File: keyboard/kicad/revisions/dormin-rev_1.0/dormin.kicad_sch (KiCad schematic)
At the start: 115 parts, among them J1 Conn_01x06, J2 Conn_01x04, J3 Conn_01x05, Q1 AO3400A, Q2 AO3407A, SW1 SW_Push, SW10 SW_Push, SW11 SW_Push, SW12 SW_Push, SW13 SW_Push, SW14 SW_Push, SW15 SW_Push, SW16 SW_Push, SW17 SW_Push, SW18 SW_Push, SW19 SW_Push, SW2 SW_Push, SW20 SW_Push, SW3 SW_Push, SW4 SW_Push, SW5 SW_Push, SW6 SW_Push, SW7 SW_Push, SW8 SW_Push, SW9 SW_Push, U3 XIAO-nRF52840-Plus-SMD, U4 TPD2E2U06DCK

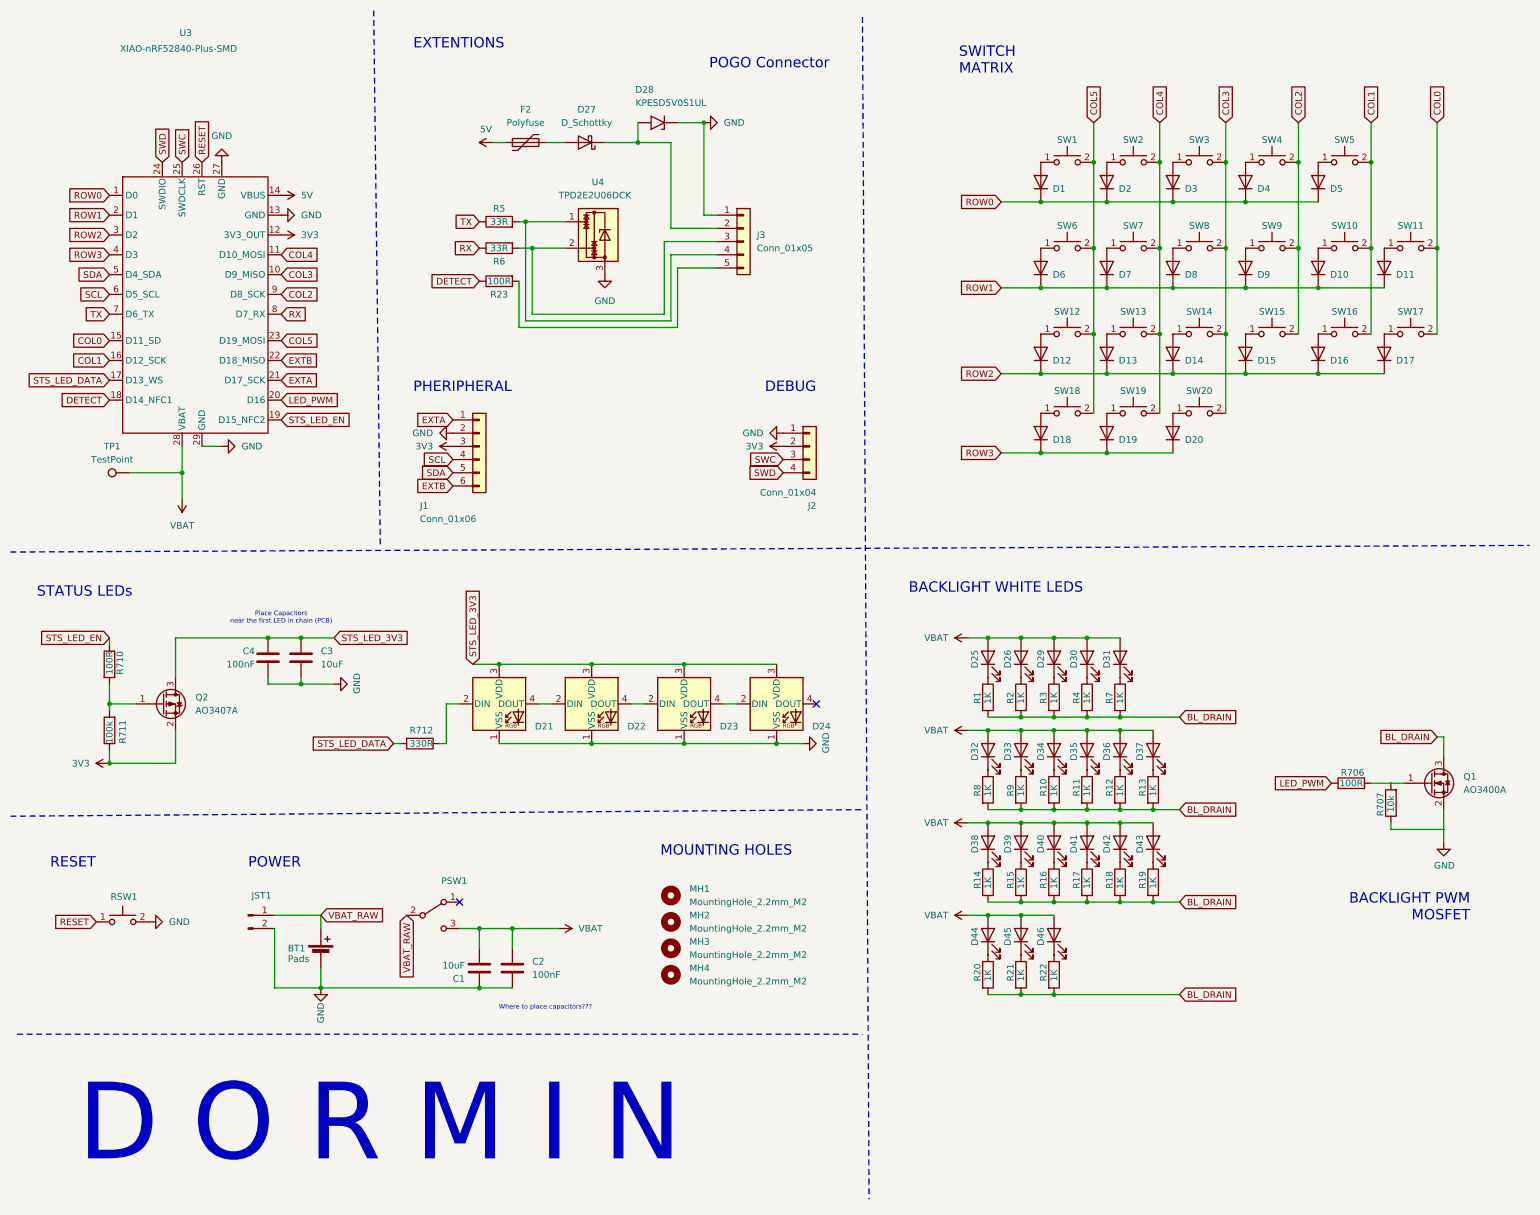
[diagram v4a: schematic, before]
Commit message: feat: improve schematics and pcb components placements
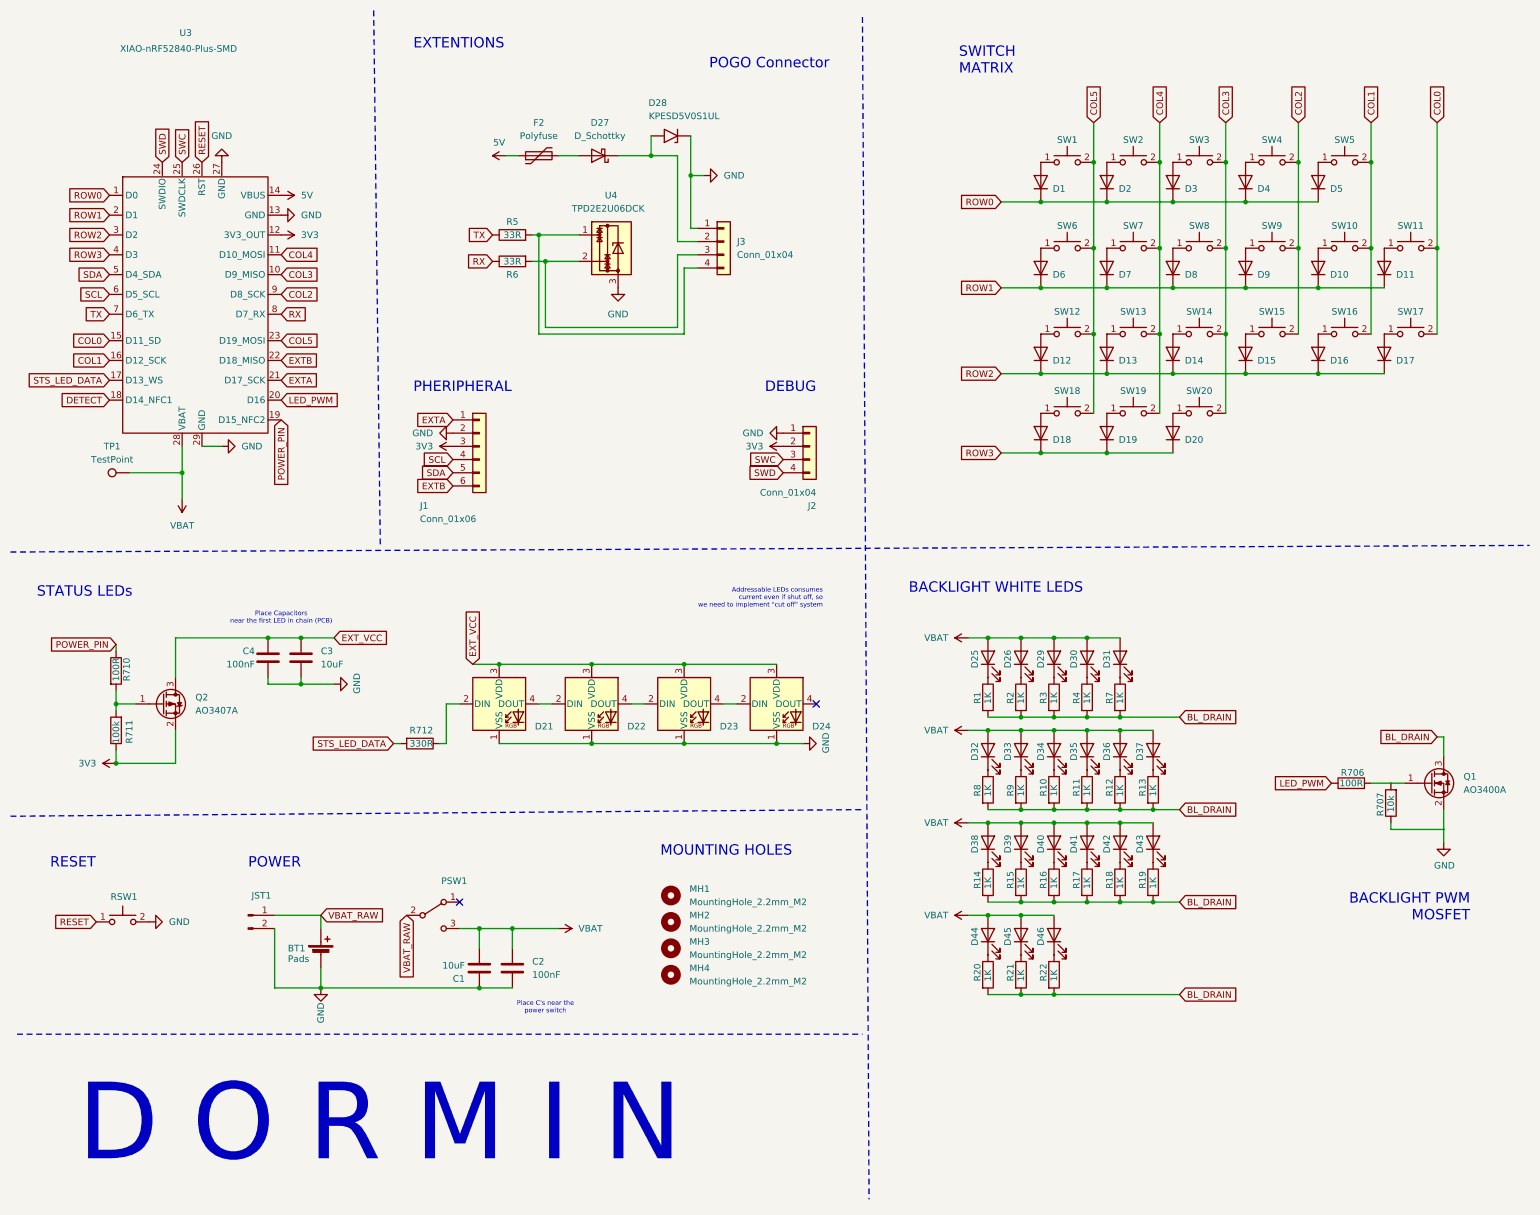
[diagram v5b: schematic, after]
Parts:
- removed J3: Conn_01x05, willkeebs_misc:SMD_Conn_1x04_P2.54mm_Vertical, symbol Connector_Generic:Conn_01x05
- removed R23: 100R, Resistor_SMD:R_0603_1608Metric, symbol Device:R
- added J3: Conn_01x04, symbol Connector_Generic:Conn_01x04
- JST1: footprint willkeebs_power:JST_1.25mm -> Connector_JST:JST_GH_SM02B-GHS-TB_1x02-1MP_P1.25mm_Horizontal; MFPN (none) -> C22074
- PSW1: footprint willkeebs_power:Switch_MSK12C02 -> PCM_marbastlib-various:SW_MSK12C02-HB; MFPN (none) -> MK-12C02-G025
- RSW1: footprint willkeebs_components:SW_Push_1P1T_XKB_TS-1187A -> Button_Switch_SMD:SW_SPST_SKQG_WithStem
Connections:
- net GND: now also J3.1 (Pin_1)
- net at R5.2, U4.1: now also J3.4 (Pin_4)
- net at D27.1 (K), D28.2 (A2): now also J3.2 (Pin_2)
- net at R6.2, U4.2: now also J3.3 (Pin_3)
- net STS_LED_3V3 renamed EXT_VCC
- net STS_LED_EN renamed POWER_PIN
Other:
- note added: "Addressable LEDs consumes current even if shut off, so we need to implement "cut off" system"
- note added: "Place C's near the power switch"
- note removed: "Where to place capacitors???"
- moved on the sheet: D27, D28, F2, R5, R6, R710, R711, U4

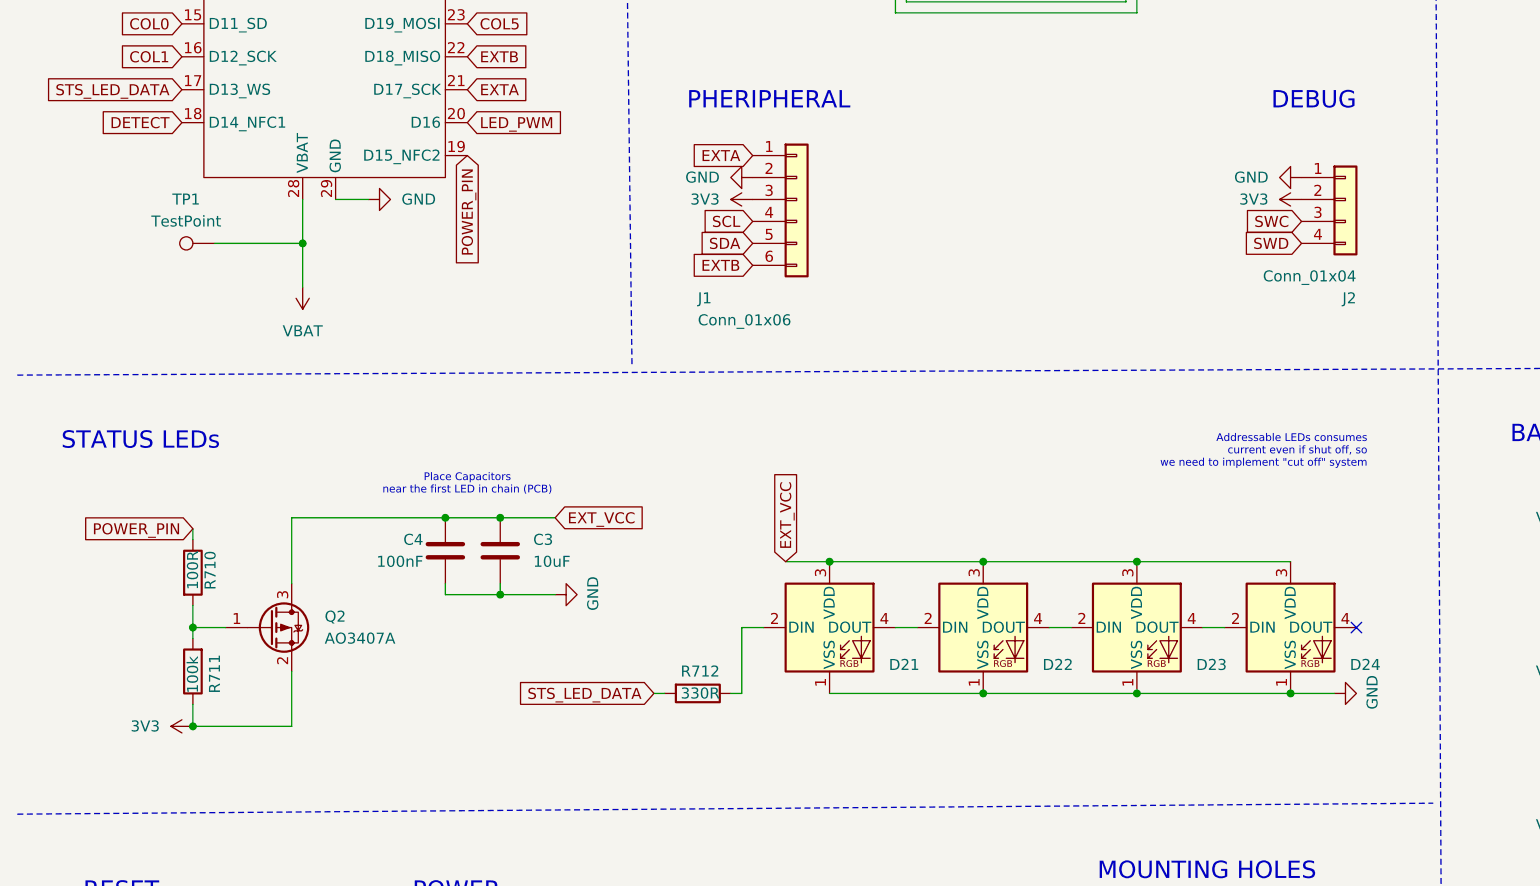
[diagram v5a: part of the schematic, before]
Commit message: feat: improve schematics and components placement
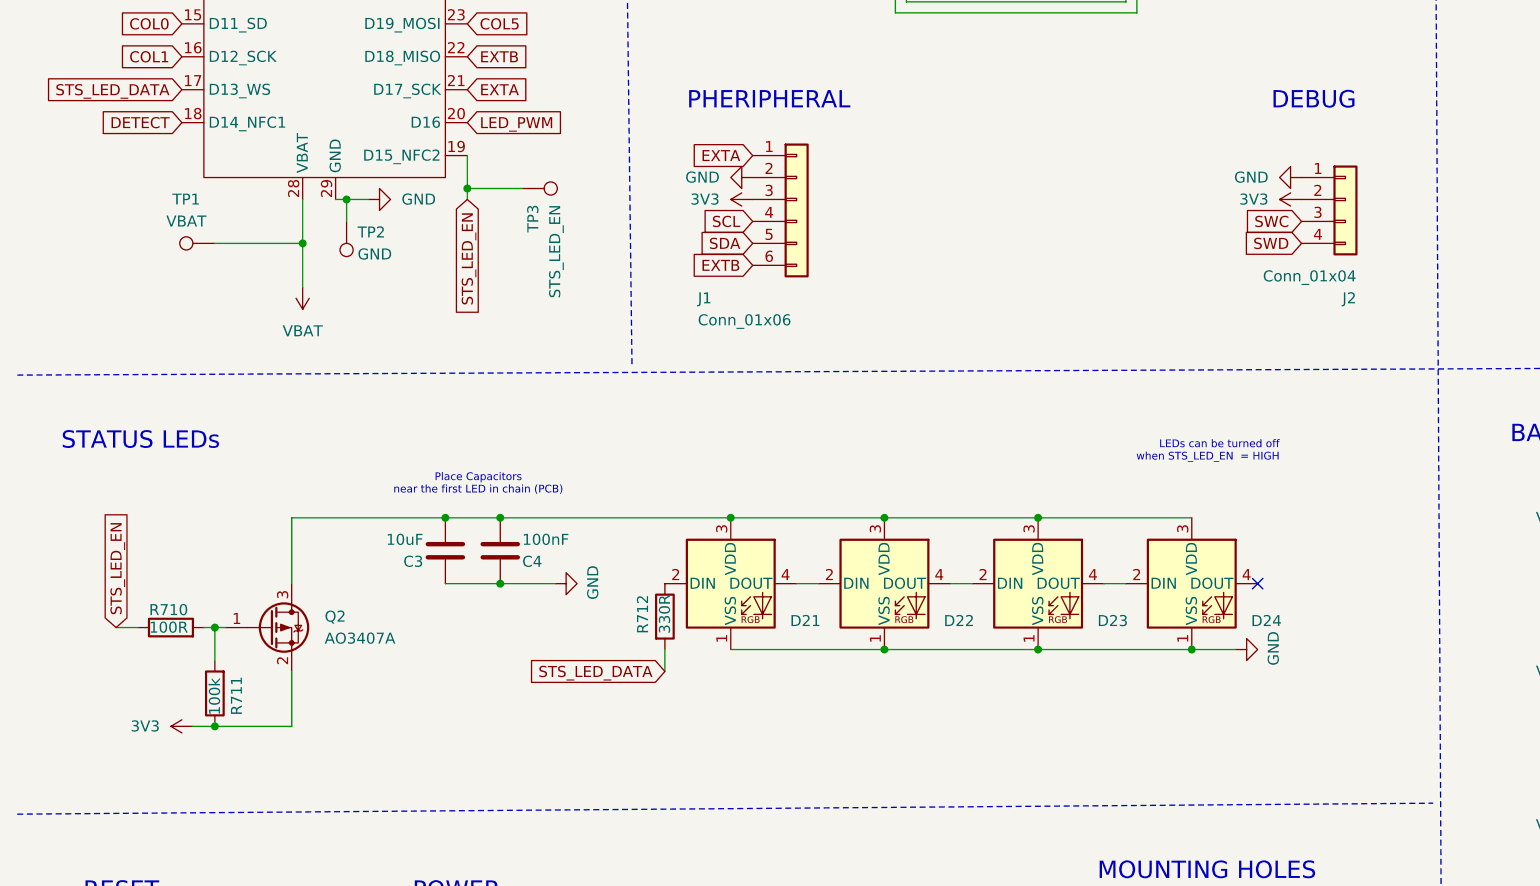
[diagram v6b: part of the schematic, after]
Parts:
- added TP2: GND, TestPoint:TestPoint_Pad_D1.0mm, symbol Connector:TestPoint
- added TP3: STS_LED_EN, TestPoint:TestPoint_Pad_D1.0mm, symbol Connector:TestPoint
- J3: footprint (none) -> willkeebs_misc:SMD_Conn_1x04_P2.54mm_Vertical
- TP1: value TestPoint -> VBAT; footprint (none) -> TestPoint:TestPoint_Pad_D1.0mm
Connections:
- net GND: now also TP2.1
- net EXT_VCC: no longer names the net of C3.2, C4.1, D21.3 (VDD), D22.3 (VDD), D23.3 (VDD), D24.3 (VDD), Q2.3 (D)
- net POWER_PIN renamed STS_LED_EN
- net STS_LED_EN: now also TP3.1
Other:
- note added: "LEDs can be turned off when STS_LED_EN = HIGH"
- note removed: "Addressable LEDs consumes current even if shut off, so we need to implement "cut off" system"
- moved on the sheet: D21, D22, D23, D24, R710, R712

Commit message: chore: added right sheet schematics
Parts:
- removed BT1: Pads, willkeebs_power:Battery_Pad, symbol Device:Battery_Cell
- removed C1, C3: 10uF, Capacitor_SMD:C_0603_1608Metric, symbol Device:C
- removed C2, C4: 100nF, Capacitor_SMD:C_0603_1608Metric, symbol Device:C
- removed D1, D10, D11, D12, D13, D14, D15, D16, D17, D18, D19, D2, D20, D3, D4, D5, D6, D7, D8, D9: 1N4148W, Diode_SMD:D_SOD-123, symbol Diode:1N4148W
- removed D21, D22, D23, D24: SK6812MINI-E, LED_SMD:LED_SK6812MINI-E_3.2x2.8mm_P1.5mm_ReverseMount, symbol LED:SK6812MINI-E
- removed D25, D26, D29, D30, D31, D32, D33, D34, D35, D36, D37, D38, D39, D40, D41, D42, D43, D44, D45, D46: LED, willkeebs_components:LED_MHT151WDT, symbol Device:LED
- removed D27: D_Schottky, Diode_SMD:D_SOD-523, symbol Device:D_Schottky
- removed D28: KPESD5V0S1UL, Diode_SMD:D_SOD-882, symbol Diode:SMF5V0A
- removed F2: Polyfuse, Fuse:Fuse_1206_3216Metric, symbol Device:Polyfuse
- removed J1: Conn_01x06, willkeebs_misc:SMD_Conn_1x06_P2.54mm_Vertical, symbol Connector_Generic:Conn_01x06
- removed J2: Conn_01x04, Connector_PinSocket_2.54mm:PinSocket_1x04_P2.54mm_Vertical, symbol Connector_Generic:Conn_01x04
- removed J3: Conn_01x04, willkeebs_misc:SMD_Conn_1x04_P2.54mm_Vertical, symbol Connector_Generic:Conn_01x04
- removed JST1: Conn_01x02_Pin, Connector_JST:JST_GH_SM02B-GHS-TB_1x02-1MP_P1.25mm_Horizontal, symbol Connector:Conn_01x02_Pin
- removed MH1, MH2, MH3, MH4: MountingHole_2.2mm_M2, MountingHole:MountingHole_2.2mm_M2, symbol Mechanical:MountingHole
- removed PSW1: SW_SPDT, PCM_marbastlib-various:SW_MSK12C02-HB, symbol Switch:SW_SPDT
- removed Q1: AO3400A, Package_TO_SOT_SMD:SOT-23, symbol Transistor_FET:AO3400A
- removed Q2: AO3407A, Package_TO_SOT_SMD:SOT-23, symbol Transistor_FET:AO3401A
- removed R1, R10, R11, R12, R13, R14, R15, R16, R17, R18, R19, R2, R20, R21, R22, R3, R4, R7, R8, R9: 1K, Resistor_SMD:R_0603_1608Metric, symbol Device:R
- removed R5, R6: 33R, Resistor_SMD:R_0603_1608Metric, symbol Device:R
- removed R706, R710: 100R, Resistor_SMD:R_0603_1608Metric, symbol Device:R
- removed R707: 10k, Resistor_SMD:R_0603_1608Metric, symbol Device:R
- removed R711: 100k, Resistor_SMD:R_0603_1608Metric, symbol Device:R
- removed R712: 330R, Resistor_SMD:R_0603_1608Metric, symbol Device:R
- removed RSW1: RSW1, Button_Switch_SMD:SW_SPST_SKQG_WithStem, symbol Switch:SW_Push
- removed SW1, SW10, SW11, SW12, SW13, SW14, SW15, SW16, SW17, SW18, SW19, SW2, SW20, SW3, SW4, SW5, SW6, SW7, SW8, SW9: SW_Push, willkeebs_keyboard:NF_LED_1206_SW_KS33_3_0_HS_1U, symbol Switch:SW_Push
- removed TP1: VBAT, TestPoint:TestPoint_Pad_D1.0mm, symbol Connector:TestPoint
- removed TP2: GND, TestPoint:TestPoint_Pad_D1.0mm, symbol Connector:TestPoint
- removed TP3: STS_LED_EN, TestPoint:TestPoint_Pad_D1.0mm, symbol Connector:TestPoint
- removed U3: XIAO-nRF52840-Plus-SMD, Seeed_Studio_XIAO_Series:XIAO-nRF52840-Plus-SMD, symbol Seeed_Studio_XIAO_Series:XIAO-nRF52840_Plus_SMD
- removed U4: TPD2E2U06DCK, Package_TO_SOT_SMD:SOT-323_SC-70, symbol Power_Protection:TPD2E2U06DCK
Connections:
- no-connect marks 2 -> 0
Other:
- added sheet Left (dormin_left.kicad_sch)
- added sheet Right (dormin_right.kicad_sch)
- note removed: "BACKLIGHT PWM MOSFET"
- note removed: "BACKLIGHT WHITE LEDS"
- note removed: "D O R M I N"
- note removed: "DEBUG"
- note removed: "EXTENTIONS"
- note removed: "LEDs can be turned off when STS_LED_EN = HIGH"
- note removed: "MOUNTING HOLES"
- note removed: "PHERIPHERAL"
- note removed: "POGO Connector"
- note removed: "POWER"
- note removed: "Place C's near the power switch"
- note removed: "Place Capacitors near the first LED in chain (PCB)"
- note removed: "RESET"
- note removed: "STATUS LEDs"
- note removed: "SWITCH MATRIX"
